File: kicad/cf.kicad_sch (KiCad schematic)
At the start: 4 parts, among them J3 Compact Flash

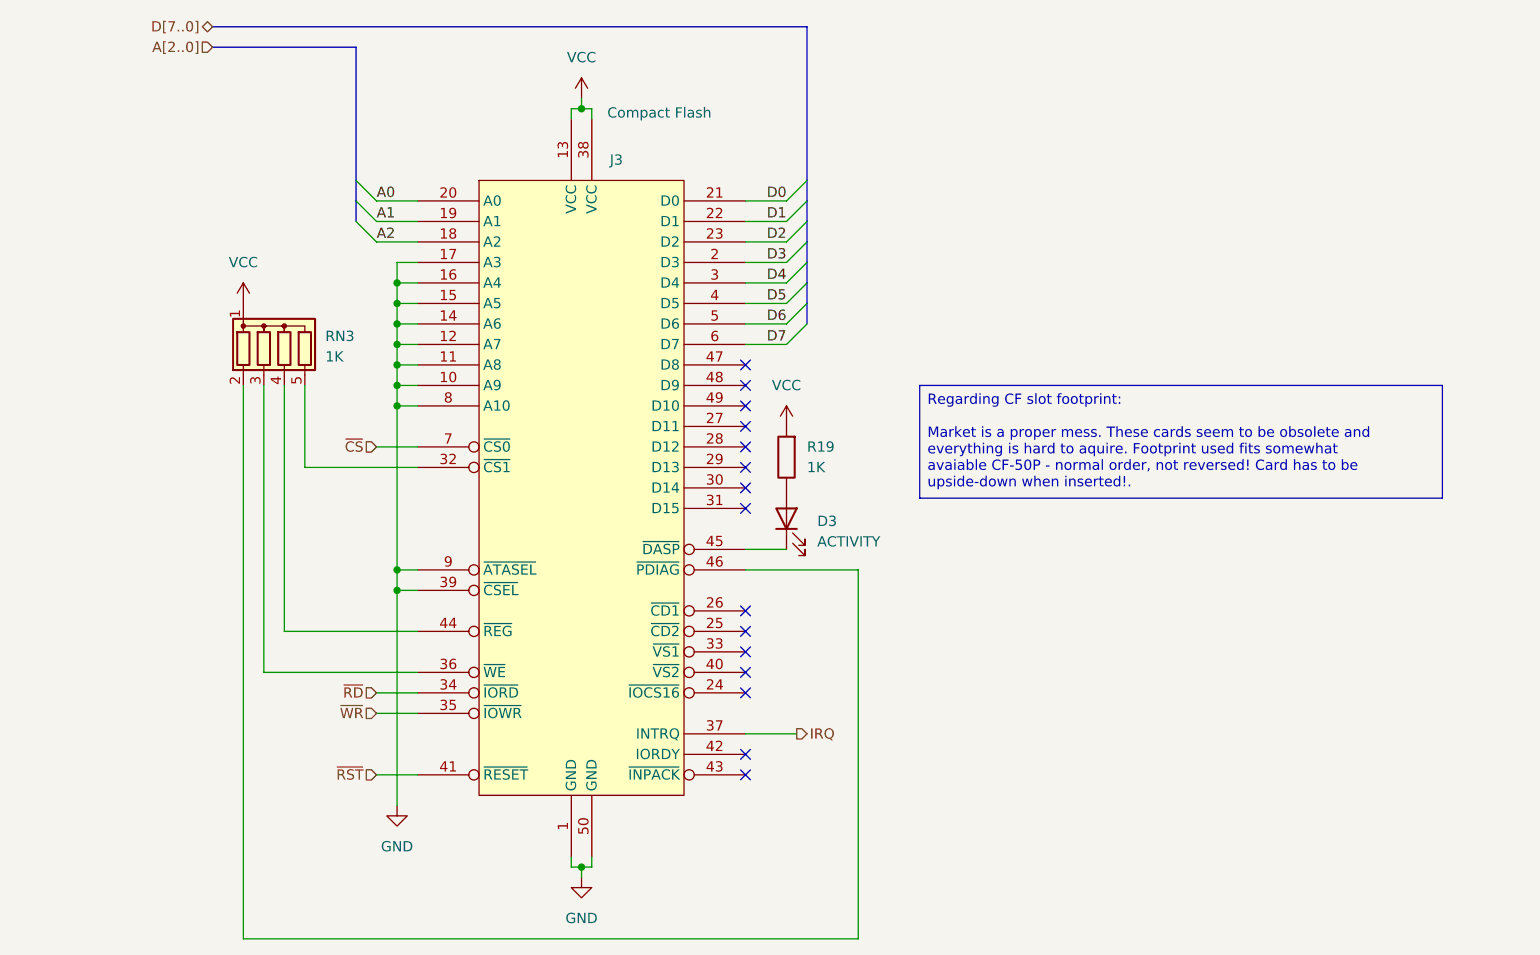
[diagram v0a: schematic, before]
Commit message: hw: add RC to /RD for CF for increased compatibility
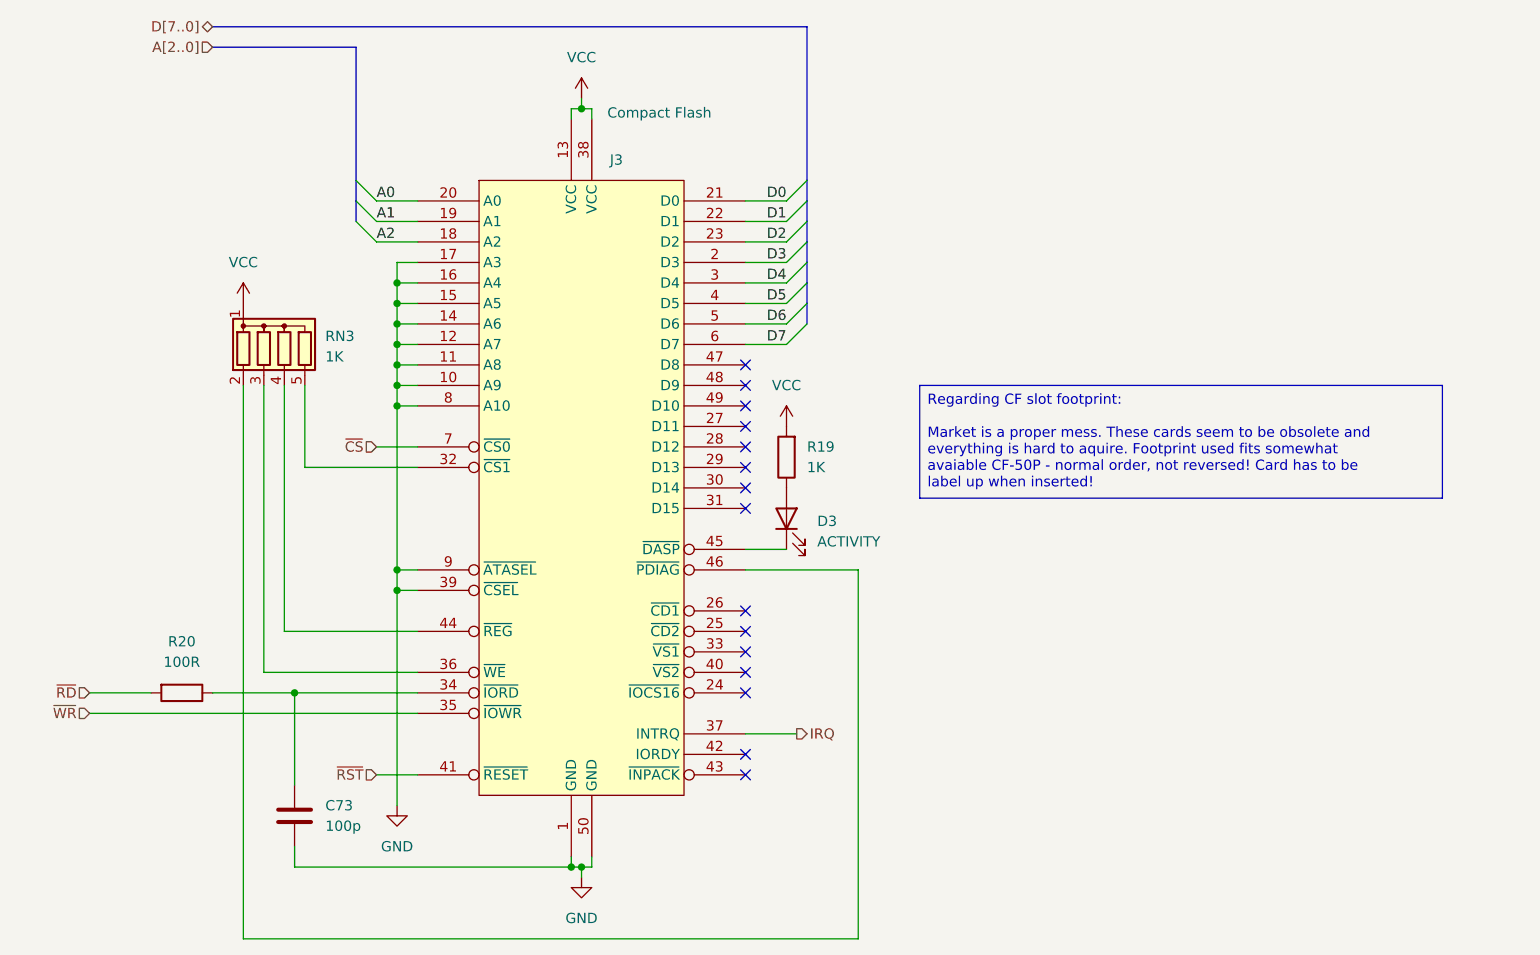
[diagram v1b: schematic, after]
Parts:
- added C73: 100p, Capacitor_THT:C_Disc_D5.0mm_W2.5mm_P2.50mm, symbol Device:C
- added R20: 100R, Resistor_THT:R_Axial_DIN0207_L6.3mm_D2.5mm_P7.62mm_Horizontal, symbol Device:R
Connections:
- net GND: now also C73.2
- net ~{RD}: now also R20.2; no longer J3.34 (~{IORD})
- new net: C73.1, J3.34 (~{IORD}), R20.1
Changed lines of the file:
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@@
 		(company "A.K.")
 	)
-	(text_box "Regarding CF slot footprint:\n\nMarket is a proper mess. These cards seem to be obsolete and\neverything is hard to aquire. Footprint used fits somewhat\navaiable CF-50P - normal order, not reversed! Card has to be\nupside-down when inserted!."
+	(text_box "Regarding CF slot footprint:\n\nMarket is a proper mess. These cards seem to be obsolete and\neverything is hard to aquire. Footprint used fits somewhat\navaiable CF-50P - normal order, not reversed! Card has to be\nlabel up when inserted!"
 		(exclude_from_sim no)
 		(at 182.88 86.36 0)
@@
 	)
 	(junction
+		(at 139.7 146.05)
+		(diameter 0)
+		(color 0 0 0 0)
+	)
+	(junction
 		(at 140.97 52.07)
 		(diameter 0)
@@
 	)
 	(junction
+		(at 105.41 124.46)
+		(diameter 0)
+		(color 0 0 0 0)
+	)
+	(junction
 		(at 118.11 111.76)
 		(diameter 0)
@@
 	(wire
 		(pts
+			(xy 105.41 146.05) (xy 105.41 143.51)
+		)
+		(stroke
+			(width 0)
+			(type default)
+		)
+	)
+	(wire
+		(pts
 			(xy 139.7 146.05) (xy 139.7 144.78)
 		)
@@
 	(wire
 		(pts
+			(xy 139.7 146.05) (xy 105.41 146.05)
+		)
+		(stroke
+			(width 0)
+			(type default)
+		)
+	)
+	(wire
+		(pts
 			(xy 120.65 96.52) (xy 106.68 96.52)
 		)
@@
 	(wire
 		(pts
+			(xy 80.01 124.46) (xy 87.63 124.46)
+		)
+		(stroke
+			(width 0)
+			(type default)
+		)
+	)
+	(wire
+		(pts
 			(xy 118.11 73.66) (xy 118.11 76.2)
 		)
@@
 	(wire
 		(pts
-			(xy 115.57 127) (xy 120.65 127)
+			(xy 80.01 127) (xy 120.65 127)
 		)
 		(stroke
@@
 	(wire
 		(pts
+			(xy 95.25 124.46) (xy 105.41 124.46)
+		)
+		(stroke
+			(width 0)
+			(type default)
+		)
+	)
+	(wire
+		(pts
 			(xy 161.29 76.2) (xy 166.37 76.2)
 		)
@@
 		)
 	)
+	(wire
+		(pts
+			(xy 105.41 124.46) (xy 105.41 135.89)
+		)
+		(stroke
+			(width 0)
+			(type default)
+		)
+	)
 	(bus
 		(pts
@@
 	(wire
 		(pts
-			(xy 115.57 124.46) (xy 120.65 124.46)
-		)
-		(stroke
-			(width 0)
-			(type default)
-		)
-	)
-	(wire
-		(pts
 			(xy 101.6 86.36) (xy 101.6 121.92)
 		)
@@
 		(pts
 			(xy 104.14 86.36) (xy 104.14 116.84)
+		)
+		(stroke
+			(width 0)
+			(type default)
+		)
+	)
+	(wire
+		(pts
+			(xy 105.41 124.46) (xy 120.65 124.46)
 		)
 		(stroke
@@
 	(hierarchical_label "~{RD}"
 		(shape input)
-		(at 115.57 124.46 180)
+		(at 80.01 124.46 180)
 		(effects
 			(font
@@
 	(hierarchical_label "~{WR}"
 		(shape input)
-		(at 115.57 127 180)
+		(at 80.01 127 180)
 		(effects
 			(font
@@
 	)
 	(symbol
+		(lib_id "Device:R")
+		(at 91.44 124.46 270)
+		(unit 1)
+		(exclude_from_sim no)
+		(in_bom yes)
+		(on_board yes)
+		(dnp no)
+		(fields_autoplaced yes)
+		(property "Reference" "R20"
+			(at 91.44 118.11 90)
+			(effects
+				(font
+					(size 1.27 1.27)
+				)
+			)
+		)
+		(property "Value" "100R"
+			(at 91.44 120.65 90)
+			(effects
+				(font
+					(size 1.27 1.27)
+				)
+			)
+		)
+		(property "Footprint" "Resistor_THT:R_Axial_DIN0207_L6.3mm_D2.5mm_P7.62mm_Horizontal"
+			(at 91.44 122.682 90)
+			(effects
+				(font
+					(size 1.27 1.27)
+				)
+				(hide yes)
+			)
+		)
+		(property "Datasheet" "~"
+			(at 91.44 124.46 0)
+			(effects
+				(font
+					(size 1.27 1.27)
+				)
+				(hide yes)
+			)
+		)
+		(property "Description" ""
+			(at 91.44 124.46 0)
+			(effects
+				(font
+					(size 1.27 1.27)
+				)
+				(hide yes)
+			)
+		)
+		(pin "2"
+		)
+		(pin "1"
+		)
+		(instances
+			(project "zak181"
+				(path "/ca48b56d-33a4-442b-b1b9-aaf2c2c8d68d/ff100799-dc4e-4ffb-ba53-ee76ebdbac69"
+					(reference "R20")
+					(unit 1)
+				)
+			)
+		)
+	)
+	(symbol
 		(lib_id "cf:CF")
 		(at 140.97 99.06 0)
@@
 					(unit 1)
 				)
+			)
+		)
+	)
+	(symbol
+		(lib_id "Device:C")
+		(at 105.41 139.7 0)
+		(unit 1)
+		(exclude_from_sim no)
+		(in_bom yes)
+		(on_board yes)
+		(dnp no)
+		(fields_autoplaced yes)
+		(property "Reference" "C73"
+			(at 109.22 138.4299 0)
+			(effects
+				(font
+					(size 1.27 1.27)
+				)
+				(justify left)
+			)
+		)
+		(property "Value" "100p"
+			(at 109.22 140.9699 0)
+			(effects
+				(font
+					(size 1.27 1.27)
+				)
+				(justify left)
+			)
+		)
+		(property "Footprint" "Capacitor_THT:C_Disc_D5.0mm_W2.5mm_P2.50mm"
+			(at 106.3752 143.51 0)
+			(effects
+				(font
+					(size 1.27 1.27)
+				)
+				(hide yes)
+			)
+		)
+		(property "Datasheet" "~"
+			(at 105.41 139.7 0)
+			(effects
+				(font
+					(size 1.27 1.27)
+				)
+				(hide yes)
+			)
+		)
+		(property "Description" "Unpolarized capacitor"
+			(at 105.41 139.7 0)
+			(effects
+				(font
+					(size 1.27 1.27)
+				)
+				(hide yes)
+			)
+		)
+		(pin "2"
+		)
+		(pin "1"
+		)
+		(instances
+			(project "zak181"
+				(path "/ca48b56d-33a4-442b-b1b9-aaf2c2c8d68d/ff100799-dc4e-4ffb-ba53-ee76ebdbac69"
+					(reference "C73")
+					(unit 1)
+				)
